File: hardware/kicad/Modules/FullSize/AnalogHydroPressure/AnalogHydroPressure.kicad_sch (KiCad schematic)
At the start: 6 parts, among them J1 Conn_02x07_Odd_Even, SW1 SW_DPDT_x2, U1 24AA025E-OT

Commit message: Fix EEPROM values and DuoRelay R5 footprint
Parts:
- U1: value 24AA025E-OT -> 24AA025E64T-I/OT
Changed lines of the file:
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@@
 			)
 		)
-		(property "Value" "24AA025E-OT"
+		(property "Value" "24AA025E64T-I/OT"
 			(at 176.1333 59.69 0)
 			(show_name no)

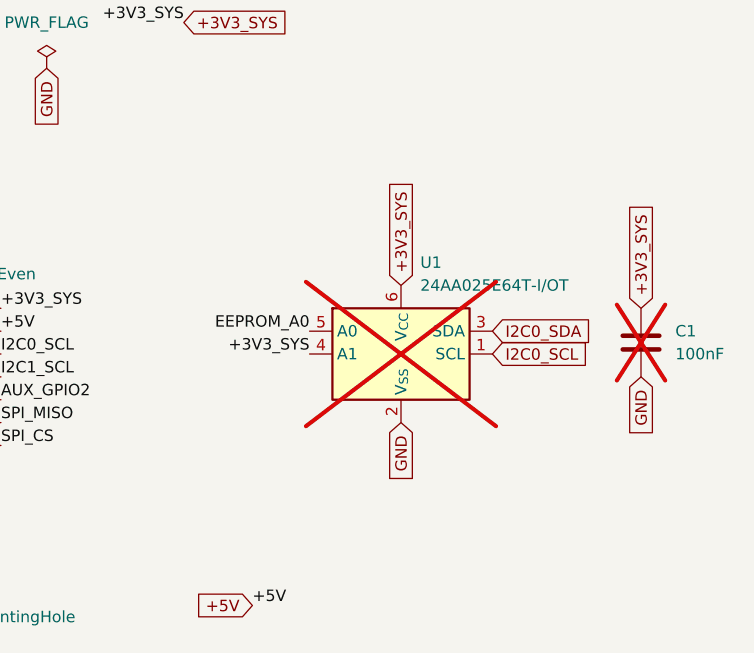
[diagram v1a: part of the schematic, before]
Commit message: Complete Rev 0.3 module schematics
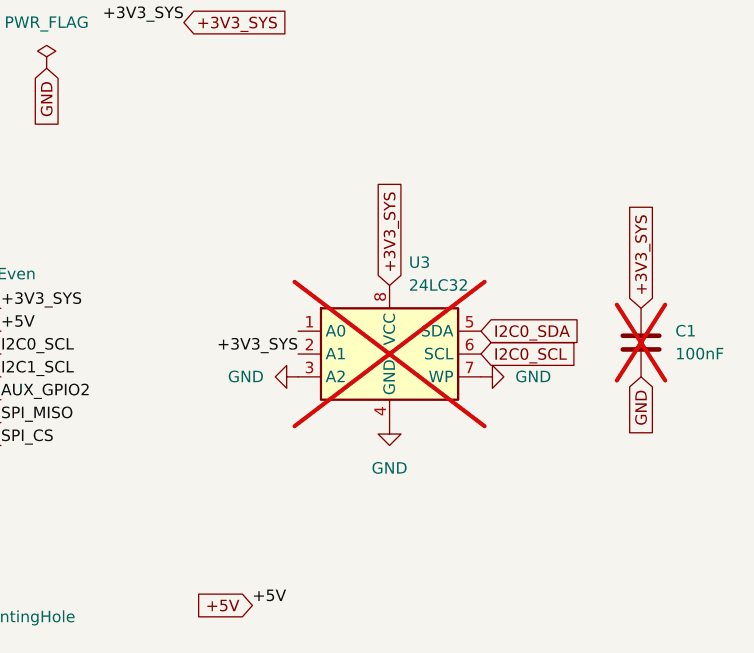
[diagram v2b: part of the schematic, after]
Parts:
- removed U1: 24AA025E64T-I/OT, Package_TO_SOT_SMD:SOT-23-6, symbol Memory_EEPROM:24AA025E-OT
- added U3: 24LC32, Package_SO:SOIC-8_3.9x4.9mm_P1.27mm, symbol Memory_EEPROM:24LC32
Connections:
- net +3V3_SYS: now also U3.2 (A1), U3.8 (VCC)
- net GND: now also U3.3 (A2), U3.4 (GND), U3.7 (WP)
- net I2C0_SCL: now also U3.6 (SCL)
- net I2C0_SDA: now also U3.5 (SDA)

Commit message: AnalogHydroPressure: update to Rev 0.4
- replace I2C bus selection switch with solder jumpers
- upgrade boost Schottky diode to B260S1F-7 (60 V, 2 A, SOD-123F)
- add test points for GND, 24V, Loop_Return and AIN0
- update PCB layout for revised components
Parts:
- removed SW1: SW_DPDT_x2, EnvNode-Footprints:SW_Slide_CK_OS202011MS2QS1, symbol Switch:SW_DPDT_x2
- added JP5, JP6: SolderJumper_3_Open, Jumper:SolderJumper-3_P1.3mm_Open_RoundedPad1.0x1.5mm_NumberLabels, symbol Jumper:SolderJumper_3_Open
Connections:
- net EEPROM_A0: now also U3.1 (A0)
- net I2C0_SCL: now also JP6.1 (A)
- net I2C0_SDA: now also JP5.1 (A)
- net I2C1_SCL: now also JP6.3 (B)
- net I2C1_SDA: now also JP5.3 (B)
- net SCL: now also JP6.2 (C)
- net SDA: now also JP5.2 (C)
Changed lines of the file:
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@@
 	(generator_version "10.0")
 	(paper "A4")
-	(label "I2C0_SDA"
-		(at 66.04 60.96 0)
+	(label "I2C1_SDA"
+		(at 64.77 36.83 0)
 		(effects
 			(font
@@
 		)
 	)
+	(label "SCL"
+		(at 59.69 59.69 270)
+		(effects
+			(font
+				(size 1.27 1.27)
+			)
+			(justify right bottom)
+		)
+	)
+	(label "I2C0_SCL"
+		(at 54.61 55.88 180)
+		(effects
+			(font
+				(size 1.27 1.27)
+			)
+			(justify right bottom)
+		)
+	)
 	(label "I2C0_SDA"
 		(at 116.84 67.31 180)
@@
 		)
 	)
+	(label "I2C0_SDA"
+		(at 54.61 36.83 180)
+		(effects
+			(font
+				(size 1.27 1.27)
+			)
+			(justify right bottom)
+		)
+	)
 	(label "SPI_SCK"
 		(at 116.84 77.47 180)
@@
 		)
 	)
+	(label "EEPROM_A0"
+		(at 162.56 64.77 180)
+		(effects
+			(font
+				(size 1.27 1.27)
+			)
+			(justify right bottom)
+		)
+	)
+	(label "SDA"
+		(at 59.69 40.64 270)
+		(effects
+			(font
+				(size 1.27 1.27)
+			)
+			(justify right bottom)
+		)
+	)
 	(label "I2C1_SCL"
-		(at 66.04 82.55 0)
+		(at 64.77 55.88 0)
 		(effects
 			(font
@@
 		)
 	)
-	(label "I2C0_SCL"
-		(at 66.04 77.47 0)
-		(effects
-			(font
-				(size 1.27 1.27)
-			)
-			(justify left bottom)
-		)
-	)
-	(label "I2C1_SDA"
-		(at 66.04 66.04 0)
-		(effects
-			(font
-				(size 1.27 1.27)
-			)
-			(justify left bottom)
-		)
-	)
 	(label "SCL"
 		(at 52.07 102.87 180)
@@
 		)
 	)
-	(label "SDA"
-		(at 55.88 63.5 180)
-		(effects
-			(font
-				(size 1.27 1.27)
-			)
-			(justify right bottom)
-		)
-	)
 	(label "AUX_GPIO1"
 		(at 52.07 143.51 180)
-		(effects
-			(font
-				(size 1.27 1.27)
-			)
-			(justify right bottom)
-		)
-	)
-	(label "SCL"
-		(at 55.88 80.01 180)
 		(effects
 			(font
@@
 	)
 	(symbol
-		(lib_id "Switch:SW_DPDT_x2")
-		(at 60.96 80.01 0)
-		(unit 2)
+		(lib_id "Jumper:SolderJumper_3_Open")
+		(at 59.69 36.83 0)
+		(unit 1)
 		(body_style 1)
 		(exclude_from_sim no)
-		(in_bom yes)
+		(in_bom no)
 		(on_board yes)
 		(in_pos_files yes)
 		(dnp no)
 		(fields_autoplaced yes)
-		(property "Reference" "SW1"
-			(at 60.96 71.12 0)
-			(show_name no)
-			(do_not_autoplace no)
-			(effects
-				(font
-					(size 1.27 1.27)
-				)
-			)
-		)
-		(property "Value" "SW_DPDT_x2"
-			(at 60.96 73.66 0)
-			(show_name no)
-			(do_not_autoplace no)
-			(effects
-				(font
-					(size 1.27 1.27)
-				)
-			)
-		)
-		(property "Footprint" "EnvNode-Footprints:SW_Slide_CK_OS202011MS2QS1"
-			(at 60.96 80.01 0)
+		(property "Reference" "JP5"
+			(at 59.69 30.48 0)
+			(show_name no)
+			(do_not_autoplace no)
+			(effects
+				(font
+					(size 1.27 1.27)
+				)
+			)
+		)
+		(property "Value" "SolderJumper_3_Open"
+			(at 59.69 33.02 0)
+			(show_name no)
+			(do_not_autoplace no)
+			(effects
+				(font
+					(size 1.27 1.27)
+				)
+			)
+		)
+		(property "Footprint" "Jumper:SolderJumper-3_P1.3mm_Open_RoundedPad1.0x1.5mm_NumberLabels"
+			(at 59.69 36.83 0)
 			(hide yes)
 			(show_name no)
@@
 		)
 		(property "Datasheet" ""
-			(at 60.96 80.01 0)
-			(hide yes)
-			(show_name no)
-			(do_not_autoplace no)
-			(effects
-				(font
-					(size 1.27 1.27)
-				)
-			)
-		)
-		(property "Description" "Switch, dual pole double throw, separate symbols"
-			(at 60.96 80.01 0)
-			(hide yes)
-			(show_name no)
-			(do_not_autoplace no)
-			(effects
-				(font
-					(size 1.27 1.27)
-				)
-			)
-		)
-		(pin "6"
+			(at 59.69 52.07 0)
+			(hide yes)
+			(show_name no)
+			(do_not_autoplace no)
+			(effects
+				(font
+					(size 1.27 1.27)
+				)
+			)
+		)
+		(property "Description" "Solder Jumper, 3-pole, open"
+			(at 59.69 49.53 0)
+			(hide yes)
+			(show_name no)
+			(do_not_autoplace no)
+			(effects
+				(font
+					(size 1.27 1.27)
+				)
+			)
+		)
+		(property private "KLC_S5.1" "This is a generic symbol, it has fp-filter, but no default footprint"
+			(at 59.69 54.61 0)
+			(hide yes)
+			(show_name yes)
+			(do_not_autoplace no)
+			(effects
+				(font
+					(size 1.27 1.27)
+				)
+			)
+		)
+		(property private "KLC_S3.3" "Graphical-Symbol: thickness is 6mm, fill is background"
+			(at 59.69 57.15 0)
+			(hide yes)
+			(show_name yes)
+			(do_not_autoplace no)
+			(effects
+				(font
+					(size 1.27 1.27)
+				)
+			)
+		)
+		(pin "1"
 		)
 		(pin "3"
-		)
-		(pin "5"
-		)
-		(pin "4"
-		)
-		(pin "1"
 		)
 		(pin "2"
@@
 			(project "AnalogHydroPressure"
 				(path "/d4f5e987-f509-4ce4-9428-d20b1343f07d"
-					(reference "SW1")
-					(unit 2)
+					(reference "JP5")
+					(unit 1)
 				)
 			)
@@
 	)
 	(symbol
-		(lib_id "Switch:SW_DPDT_x2")
-		(at 60.96 63.5 0)
-		(unit 1)
-		(body_style 1)
-		(exclude_from_sim no)
-		(in_bom yes)
-		(on_board yes)
-		(in_pos_files yes)
-		(dnp no)
-		(fields_autoplaced yes)
-		(property "Reference" "SW1"
-			(at 60.96 54.61 0)
-			(show_name no)
-			(do_not_autoplace no)
-			(effects
-				(font
-					(size 1.27 1.27)
-				)
-			)
-		)
-		(property "Value" "SW_DPDT_x2"
-			(at 60.96 57.15 0)
-			(show_name no)
-			(do_not_autoplace no)
-			(effects
-				(font
-					(size 1.27 1.27)
-				)
-			)
-		)
-		(property "Footprint" "EnvNode-Footprints:SW_Slide_CK_OS202011MS2QS1"
-			(at 60.96 63.5 0)
-			(hide yes)
-			(show_name no)
-			(do_not_autoplace no)
-			(effects
-				(font
-					(size 1.27 1.27)
-				)
-			)
-		)
-		(property "Datasheet" ""
-			(at 60.96 63.5 0)
-			(hide yes)
-			(show_name no)
-			(do_not_autoplace no)
-			(effects
-				(font
-					(size 1.27 1.27)
-				)
-			)
-		)
-		(property "Description" "Switch, dual pole double throw, separate symbols"
-			(at 60.96 63.5 0)
-			(hide yes)
-			(show_name no)
-			(do_not_autoplace no)
-			(effects
-				(font
-					(size 1.27 1.27)
-				)
-			)
-		)
-		(pin "6"
-		)
-		(pin "3"
-		)
-		(pin "5"
-		)
-		(pin "4"
-		)
-		(pin "1"
-		)
-		(pin "2"
-		)
-		(instances
-			(project "AnalogHydroPressure"
-				(path "/d4f5e987-f509-4ce4-9428-d20b1343f07d"
-					(reference "SW1")
-					(unit 1)
-				)
-			)
-		)
-	)
-	(symbol
 		(lib_id "Device:C")
 		(at 200.66 66.04 0)
@@
 					(unit 1)
 				)
+			)
+		)
+	)
+	(symbol
+		(lib_id "Jumper:SolderJumper_3_Open")
+		(at 59.69 55.88 0)
+		(unit 1)
+		(body_style 1)
+		(exclude_from_sim no)
+		(in_bom no)
+		(on_board yes)
+		(in_pos_files yes)
+		(dnp no)
+		(fields_autoplaced yes)
+		(property "Reference" "JP6"
+			(at 59.69 49.53 0)
+			(show_name no)
+			(do_not_autoplace no)
+			(effects
+				(font
+					(size 1.27 1.27)
+				)
+			)
+		)
+		(property "Value" "SolderJumper_3_Open"
+			(at 59.69 52.07 0)
+			(show_name no)
+			(do_not_autoplace no)
+			(effects
+				(font
+					(size 1.27 1.27)
+				)
+			)
+		)
+		(property "Footprint" "Jumper:SolderJumper-3_P1.3mm_Open_RoundedPad1.0x1.5mm_NumberLabels"
+			(at 59.69 55.88 0)
+			(hide yes)
+			(show_name no)
+			(do_not_autoplace no)
+			(effects
+				(font
+					(size 1.27 1.27)
+				)
+			)
+		)
+		(property "Datasheet" ""
+			(at 59.69 71.12 0)
+			(hide yes)
+			(show_name no)
+			(do_not_autoplace no)
+			(effects
+				(font
+					(size 1.27 1.27)
+				)
+			)
+		)
+		(property "Description" "Solder Jumper, 3-pole, open"
+			(at 59.69 68.58 0)
+			(hide yes)
+			(show_name no)
+			(do_not_autoplace no)
+			(effects
+				(font
+					(size 1.27 1.27)
+				)
+			)
+		)
+		(property private "KLC_S5.1" "This is a generic symbol, it has fp-filter, but no default footprint"
+			(at 59.69 73.66 0)
+			(hide yes)
+			(show_name yes)
+			(do_not_autoplace no)
+			(effects
+				(font
+					(size 1.27 1.27)
+				)
+			)
+		)
+		(property private "KLC_S3.3" "Graphical-Symbol: thickness is 6mm, fill is background"
+			(at 59.69 76.2 0)
+			(hide yes)
+			(show_name yes)
+			(do_not_autoplace no)
+			(effects
+				(font
+					(size 1.27 1.27)
+				)
+			)
+		)
+		(pin "1"
+		)
+		(pin "3"
+		)
+		(pin "2"
+		)
+		(instances
+			(project "AnalogHydroPressure"
+				(path "/d4f5e987-f509-4ce4-9428-d20b1343f07d"
+					(reference "JP6")
+					(unit 1)
+				)

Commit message: hardware(hydro): move boost enable to AUX_GPIO2 in revision 0.5
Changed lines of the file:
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@@
 		)
 	)
-	(label "AUX_GPIO1"
+	(label "AUX_GPIO2"
 		(at 52.07 143.51 180)
 		(effects

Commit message: Update module EEPROM assembly and bring-up documentation
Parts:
- C1, U3: now fitted
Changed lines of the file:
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@@
 		(on_board yes)
 		(in_pos_files yes)
-		(dnp yes)
+		(dnp no)
 		(fields_autoplaced yes)
 		(property "Reference" "C1"
@@
 		(on_board yes)
 		(in_pos_files yes)
-		(dnp yes)
+		(dnp no)
 		(fields_autoplaced yes)
 		(property "Reference" "U3"
